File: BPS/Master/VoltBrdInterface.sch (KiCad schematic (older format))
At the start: 8 parts, among them J6 VoltageSlaveConnector, U8 LTC6820, U9 HX1188FNL

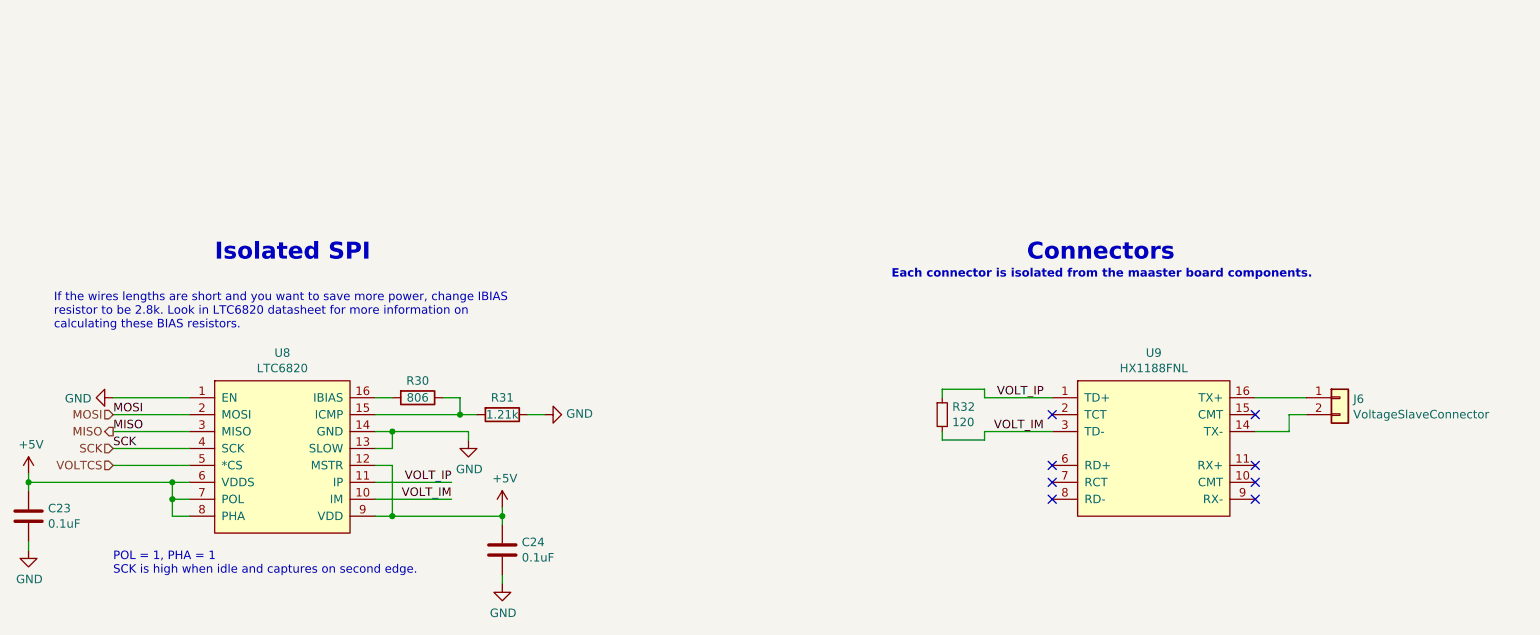
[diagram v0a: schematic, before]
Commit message: Creates fan brd interface schematics and updates symbols/footprints related to the leader board
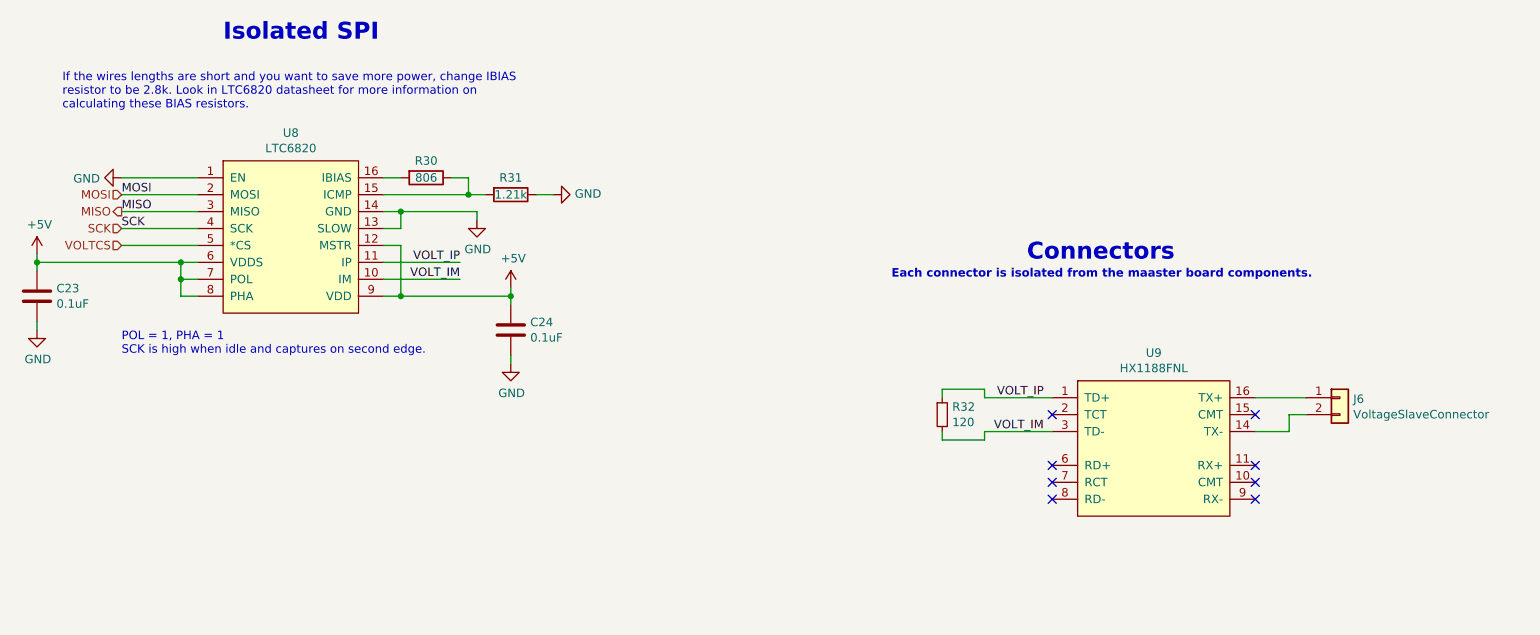
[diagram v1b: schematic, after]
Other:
- moved on the sheet: C23, C24, R30, R31, U8
